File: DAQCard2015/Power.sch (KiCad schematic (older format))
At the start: 22 parts, among them CON1 BARREL_JACK, SW1 DPDT, U20 LM1086_1V8, U21 LT1913, U25 LM1086_2V5

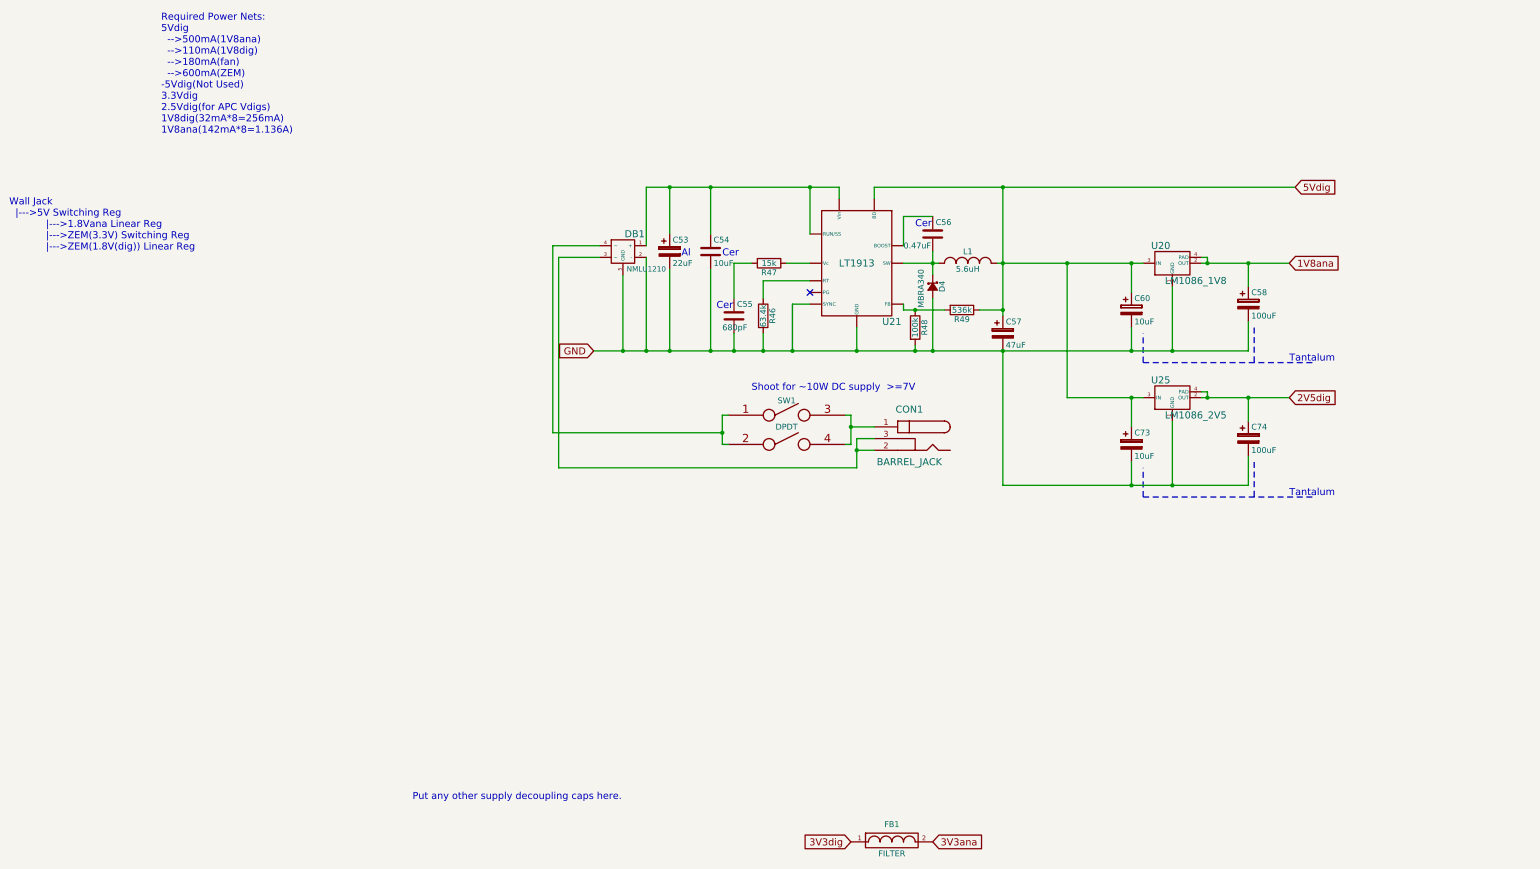
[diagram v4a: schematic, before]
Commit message: Adds digipart field to all parts that is now used in automatic generation of BOM(see DAQCard2015.html)
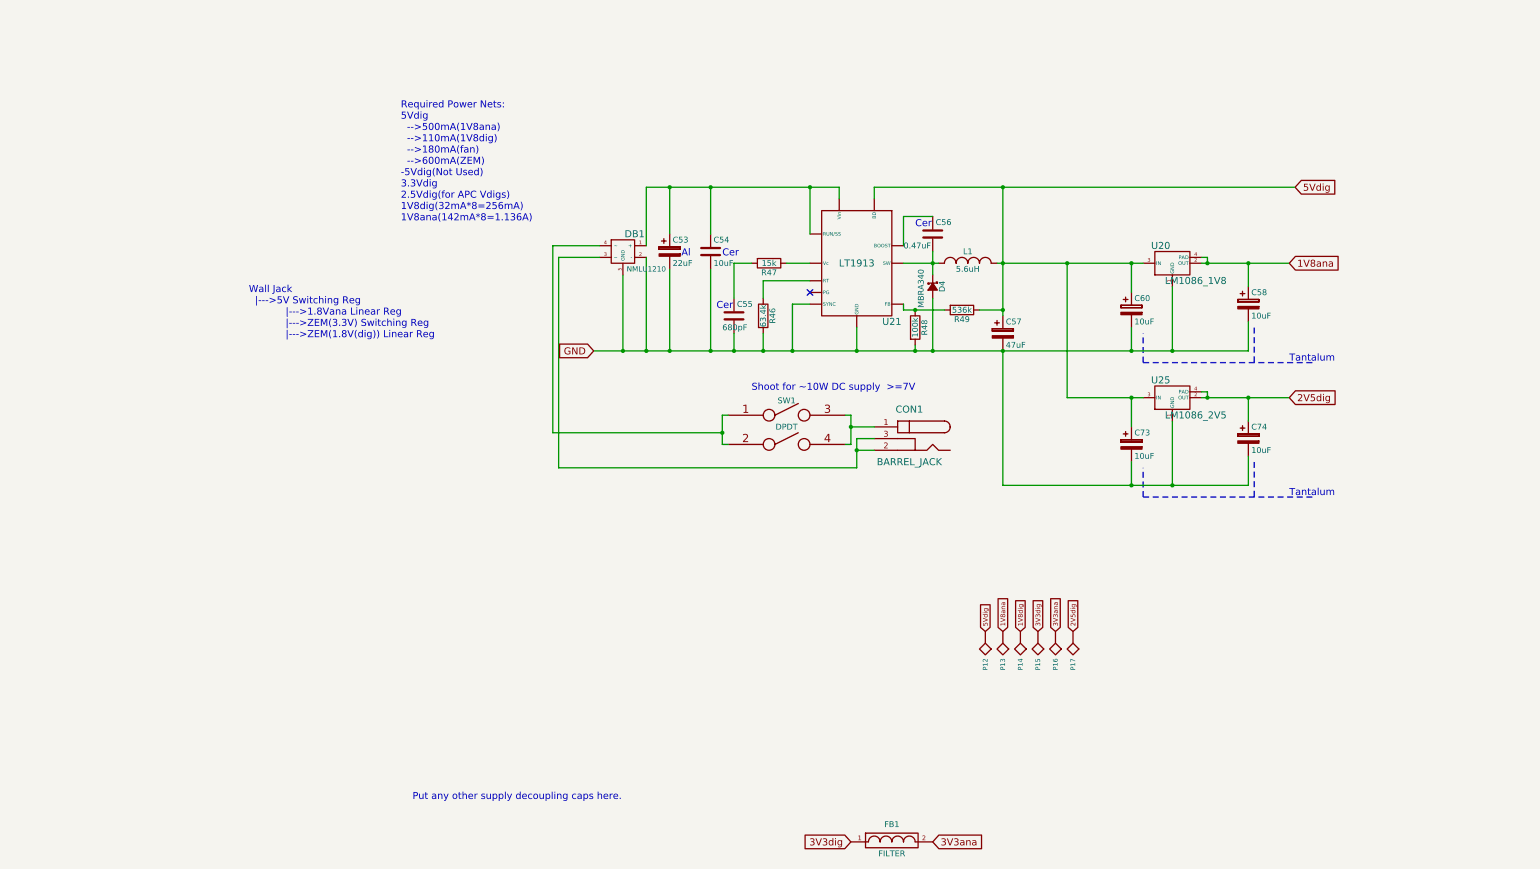
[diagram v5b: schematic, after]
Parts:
- added P12: 5Vdig, extras:testpad, symbol SPYPAD
- added P13: 1.8Vana, extras:testpad, symbol SPYPAD
- added P14: 1.8Vdig, extras:testpad, symbol SPYPAD
- added P15: 3.3Vdig, extras:testpad, symbol SPYPAD
- added P16: 3.3Vana, extras:testpad, symbol SPYPAD
- added P17: 2.5Vdig, extras:testpad, symbol SPYPAD
- C53: digipart (none) -> 493-9771-1-ND
- C54: digipart (none) -> 445-11464-1-ND
- C55: digipart (none) -> 445-1291-1-ND
- C56: digipart (none) -> 445-7464-1-ND
- C57: digipart (none) -> 478-9200-1-ND
- C58, C74: value 100uF -> 10uF; digipart (none) -> 478-3337-1-ND
- C60, C73: digipart (none) -> 478-3337-1-ND
- CON1: digipart (none) -> CP-002B-ND
- D4: digipart (none) -> MBRA340T3GOSCT-ND
- DB1: digipart (none) -> NMLU1210TWGOSCT-ND
- FB1: digipart (none) -> MH2029-070YCT-ND
- L1: digipart (none) -> 445-6477-1-ND
- R46: digipart (none) -> P63.4KHCT-ND
- R47: digipart (none) -> P15.0KHCT-ND
- R48: digipart (none) -> P100KHCT-ND
- R49: digipart (none) -> P536KHCT-ND
- SW1: digipart (none) -> CKN2062-ND
- U20: digipart (none) -> LM1086ISX-1.8/NOPBCT-ND
- U21: digipart (none) -> LT1913EDD#PBF-ND
- U25: digipart (none) -> LM1086CSX-2.5/NOPBCT-ND
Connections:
- net 1V8ana: now also P13.1
- net 2V5dig: now also P17.1
- net 3V3ana: now also P16.1
- net 3V3dig: now also P15.1
- net 5Vdig: now also P12.1
- new net 1V8dig: P14.1
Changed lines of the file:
@@
 Comment4 ""
 $EndDescr
-Text Notes -600 1050 0    60   ~ 0
+Text Notes 1450 1800 0    60   ~ 0
 Required Power Nets:\n5Vdig\n  -->500mA(1V8ana)\n  -->110mA(1V8dig)\n  -->180mA(fan)\n  -->600mA(ZEM)\n-5Vdig(Not Used)\n3.3Vdig\n2.5Vdig(for APC Vdigs)\n1V8dig(32mA*8=256mA)\n1V8ana(142mA*8=1.136A)
 Text GLabel 9050 2150 2    60   Input ~ 0
@@
 F 2 "Connect:BARREL_JACK" H 5800 3650 60  0001 C CNN
 F 3 "" H 5800 3650 60  0000 C CNN
+F 4 "CP-002B-ND" H 5800 3650 60  0001 C CNN "digipart"
 	1    5800 3650
 	-1   0    0    -1
@@
 F 2 "extras:SMD_Cap_8mmDia" H 3788 1900 30  0001 C CNN
 F 3 "" H 3750 2050 60  0000 C CNN
+F 4 "493-9771-1-ND" H 3750 2050 60  0001 C CNN "digipart"
 	1    3750 2050
 	1    0    0    -1
@@
 F 2 "Resistors_SMD:R_0805" H 5650 7100 60  0001 C CNN
 F 3 "" H 5650 7100 60  0000 C CNN
+F 4 "MH2029-070YCT-ND" H 5650 7100 60  0001 C CNN "digipart"
 	1    5650 7100
 	1    0    0    -1
@@
 F 2 "extras:TO-263-4" H 8050 2350 60  0001 C CNN
 F 3 "" H 8050 2350 60  0000 C CNN
+F 4 "LM1086ISX-1.8/NOPBCT-ND" H 8050 2350 60  0001 C CNN "digipart"
 	1    8050 2350
 	1    0    0    -1
@@
 F 2 "Capacitors_SMD:C_0805" H 4138 1900 30  0001 C CNN
 F 3 "" H 4100 2050 60  0000 C CNN
+F 4 "445-11464-1-ND" H 4100 2050 60  0001 C CNN "digipart"
 	1    4100 2050
 	1    0    0    -1
@@
 F 2 "extras:LT1913" H 3450 1700 60  0001 C CNN
 F 3 "" H 3450 1700 60  0000 C CNN
+F 4 "LT1913EDD#PBF-ND" H 5350 2150 60  0001 C CNN "digipart"
 	1    5350 2150
 	1    0    0    -1
@@
 F 2 "Capacitors_SMD:C_0603" H 4338 2450 30  0001 C CNN
 F 3 "" H 4300 2600 60  0000 C CNN
+F 4 "445-1291-1-ND" H 4300 2600 60  0001 C CNN "digipart"
 	1    4300 2600
 	1    0    0    -1
@@
 F 2 "Capacitors_SMD:C_0603" H 6038 1750 30  0001 C CNN
 F 3 "" H 6000 1900 60  0000 C CNN
+F 4 "445-7464-1-ND" H 6000 1900 60  0001 C CNN "digipart"
 	1    6000 1900
 	1    0    0    -1
@@
 F 2 "Resistors_SMD:R_0603" V 4530 2150 30  0001 C CNN
 F 3 "" H 4600 2150 30  0000 C CNN
+F 4 "P15.0KHCT-ND" V 4600 2150 60  0001 C CNN "digipart"
 	1    4600 2150
 	0    1    1    0
@@
 F 2 "Resistors_SMD:R_0603" V 4480 2600 30  0001 C CNN
 F 3 "" H 4550 2600 30  0000 C CNN
+F 4 "P63.4KHCT-ND" V 4550 2600 60  0001 C CNN "digipart"
 	1    4550 2600
 	1    0    0    -1
@@
 F 2 "Diodes_SMD:SMA_Standard" V 6000 2350 60  0001 C CNN
 F 3 "" V 6000 2350 60  0000 C CNN
+F 4 "MBRA340T3GOSCT-ND" H 6000 2350 60  0001 C CNN "digipart"
 	1    6000 2350
 	0    1    1    0
@@
 F 2 "Resistors_SMD:R_0603" V 5780 2700 30  0001 C CNN
 F 3 "" H 5850 2700 30  0000 C CNN
+F 4 "P100KHCT-ND" V 5850 2700 60  0001 C CNN "digipart"
 	1    5850 2700
 	1    0    0    -1
@@
 F 2 "Resistors_SMD:R_0603" V 6180 2550 30  0001 C CNN
 F 3 "" H 6250 2550 30  0000 C CNN
+F 4 "P536KHCT-ND" V 6250 2550 60  0001 C CNN "digipart"
 	1    6250 2550
 	0    1    1    0
@@
 F 2 "extras:SLF101" H 6300 2150 60  0001 C CNN
 F 3 "" H 6300 2150 60  0000 C CNN
+F 4 "445-6477-1-ND" H 6300 2150 60  0001 C CNN "digipart"
 	1    6300 2150
 	1    0    0    -1
 $EndComp
-Text Notes -1900 2050 0    60   ~ 0
+Text Notes 150  2800 0    60   ~ 0
 Wall Jack\n  |--->5V Switching Reg\n            |--->1.8Vana Linear Reg\n            |--->ZEM(3.3V) Switching Reg\n            |--->ZEM(1.8V(dig)) Linear Reg\n
 $Comp
@@
 F 2 "extras:NMLU1210" H 3250 1975 60  0001 C CNN
 F 3 "" H 3250 1975 60  0000 C CNN
+F 4 "NMLU1210TWGOSCT-ND" H 3350 2050 60  0001 C CNN "digipart"
 	1    3350 2050
 	-1   0    0    -1
@@
 P 8700 2500
 F 0 "C58" H 8725 2600 50  0000 L CNN
-F 1 "100uF" H 8725 2400 50  0000 L CNN
+F 1 "10uF" H 8725 2400 50  0000 L CNN
 F 2 "Capacitors_Tantalum_SMD:TantalC_SizeD_EIA-7343_Reflow" H 8738 2350 30  0001 C CNN
 F 3 "" H 8700 2500 60  0000 C CNN
+F 4 "478-3337-1-ND" H 8700 2500 60  0001 C CNN "digipart"
 	1    8700 2500
 	1    0    0    -1
@@
 F 2 "Capacitors_Tantalum_SMD:TantalC_SizeD_EIA-7343_Reflow" H 7738 2400 30  0001 C CNN
 F 3 "" H 7700 2550 60  0000 C CNN
+F 4 "478-3337-1-ND" H 7700 2550 60  0001 C CNN "digipart"
 	1    7700 2550
 	1    0    0    -1
@@
 F 2 "Capacitors_Tantalum_SMD:TantalC_SizeD_EIA-7343_Reflow" H 6638 2600 30  0001 C CNN
 F 3 "" H 6600 2750 60  0000 C CNN
+F 4 "478-9200-1-ND" H 6600 2750 60  0001 C CNN "digipart"
 	1    6600 2750
 	1    0    0    -1
@@
 F 2 "extras:TO-263-4" H 8050 3500 60  0001 C CNN
 F 3 "" H 8050 3500 60  0000 C CNN
+F 4 "LM1086CSX-2.5/NOPBCT-ND" H 8050 3500 60  0001 C CNN "digipart"
 	1    8050 3500
 	1    0    0    -1
@@
 P 8700 3650
 F 0 "C74" H 8725 3750 50  0000 L CNN
-F 1 "100uF" H 8725 3550 50  0000 L CNN
+F 1 "10uF" H 8725 3550 50  0000 L CNN
 F 2 "Capacitors_Tantalum_SMD:TantalC_SizeD_EIA-7343_Reflow" H 8738 3500 30  0001 C CNN
 F 3 "" H 8700 3650 60  0000 C CNN
+F 4 "478-3337-1-ND" H 8700 3650 60  0001 C CNN "digipart"
 	1    8700 3650
 	1    0    0    -1
@@
 F 2 "Capacitors_Tantalum_SMD:TantalC_SizeD_EIA-7343_Reflow" H 7738 3550 30  0001 C CNN
 F 3 "" H 7700 3700 60  0000 C CNN
+F 4 "478-3337-1-ND" H 7700 3700 60  0001 C CNN "digipart"
 	1    7700 3700
 	1    0    0    -1
@@
 F 2 "extras:DFXX-XX-X-XX-A-X-XX" H 4750 3450 60  0001 C CNN
 F 3 "" H 4750 3450 60  0000 C CNN
+F 4 "CKN2062-ND" H 4750 3450 60  0001 C CNN "digipart"
 	1    4750 3450
 	1    0    0    -1
@@
 Wire Wire Line
 	2800 3900 2800 2100
+$Comp
+L SPYPAD P12
+U 1 1 560EDBF6
+P 6450 5450
+F 0 "P12" H 6530 5450 40  0000 L CNN
+F 1 "5Vdig" H 6450 5500 30  0001 C CNN
+F 2 "extras:testpad" H 6450 5450 60  0001 C CNN
+F 3 "" H 6450 5450 60  0000 C CNN
+	1    6450 5450
+	0    1    1    0
+$EndComp
+$Comp
+L SPYPAD P13
+U 1 1 560EDD25
+P 6600 5450
+F 0 "P13" H 6680 5450 40  0000 L CNN
+F 1 "1.8Vana" H 6600 5500 30  0001 C CNN
+F 2 "extras:testpad" H 6600 5450 60  0001 C CNN
+F 3 "" H 6600 5450 60  0000 C CNN
+	1    6600 5450
+	0    1    1    0
+$EndComp
+$Comp
+L SPYPAD P14
+U 1 1 560EDD7F
+P 6750 5450
+F 0 "P14" H 6830 5450 40  0000 L CNN
+F 1 "1.8Vdig" H 6750 5500 30  0001 C CNN
+F 2 "extras:testpad" H 6750 5450 60  0001 C CNN
+F 3 "" H 6750 5450 60  0000 C CNN
+	1    6750 5450
+	0    1    1    0
+$EndComp
+$Comp
+L SPYPAD P15
+U 1 1 560EDDDC
+P 6900 5450
+F 0 "P15" H 6980 5450 40  0000 L CNN
+F 1 "3.3Vdig" H 6900 5500 30  0001 C CNN
+F 2 "extras:testpad" H 6900 5450 60  0001 C CNN
+F 3 "" H 6900 5450 60  0000 C CNN
+	1    6900 5450
+	0    1    1    0
+$EndComp
+$Comp
+L SPYPAD P16
+U 1 1 560EDE3C
+P 7050 5450
+F 0 "P16" H 7130 5450 40  0000 L CNN
+F 1 "3.3Vana" H 7050 5500 30  0001 C CNN
+F 2 "extras:testpad" H 7050 5450 60  0001 C CNN
+F 3 "" H 7050 5450 60  0000 C CNN
+	1    7050 5450
+	0    1    1    0
+$EndComp
+Text GLabel 6450 5300 1    40   Input ~ 0
+5Vdig
+Text GLabel 6600 5300 1    40   Input ~ 0
+1V8ana
+Text GLabel 6750 5300 1    40   Input ~ 0
+1V8dig
+Text GLabel 6900 5300 1    40   Input ~ 0
+3V3dig
+Text GLabel 7050 5300 1    40   Input ~ 0
+3V3ana
+$Comp
+L SPYPAD P17
+U 1 1 560EE37C
+P 7200 5450
+F 0 "P17" H 7280 5450 40  0000 L CNN
+F 1 "2.5Vdig" H 7200 5500 30  0001 C CNN
+F 2 "extras:testpad" H 7200 5450 60  0001 C CNN
+F 3 "" H 7200 5450 60  0000 C CNN
+	1    7200 5450
+	0    1    1    0
+$EndComp
+Text GLabel 7200 5300 1    40   Input ~ 0
+2V5dig
 $EndSCHEMATC

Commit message: bunch of updates
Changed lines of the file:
@@
 	8300 2100 8350 2100
-Wire Wire Line
-	6550 2150 7800 2150
 Wire Wire Line
 	2800 2100 3150 2100
@@
 Wire Notes Line
 	7800 3000 7800 2750
-Wire Wire Line
-	3100 2900 8700 2900
 $Comp
 L CP C57
@@
 	6600 4050 8700 4050
 Wire Wire Line
-	7150 3300 7150 2150
+	7150 1500 7150 3300
 Connection ~ 7150 2150
 Wire Wire Line
@@
 Text GLabel 7200 5300 1    40   Input ~ 0
 2V5dig
+Wire Wire Line
+	6550 2150 6600 2150
+Connection ~ 7150 1500
+Wire Wire Line
+	7150 2150 7800 2150
+Wire Wire Line
+	3100 2900 8700 2900
 $EndSCHEMATC

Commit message: annotates parts for new build-management tool
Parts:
- C53: Digikey (none) -> 493-9771-1-ND; digipart 493-9771-1-ND -> (none)
- C54: Digikey (none) -> 445-11464-1-ND; digipart 445-11464-1-ND -> (none)
- C55: Digikey (none) -> 445-1291-1-ND; digipart 445-1291-1-ND -> (none)
- C56: Digikey (none) -> 445-7464-1-ND; digipart 445-7464-1-ND -> (none)
- C57: Digikey (none) -> 478-9200-1-ND; digipart 478-9200-1-ND -> (none)
- C58, C60, C73, C74: Digikey (none) -> 478-3337-1-ND; digipart 478-3337-1-ND -> (none)
- CON1: Digikey (none) -> CP-002B-ND; digipart CP-002B-ND -> (none)
- D4: Digikey (none) -> MBRA340T3GOSCT-ND; digipart MBRA340T3GOSCT-ND -> (none)
- DB1: Digikey (none) -> NMLU1210TWGOSCT-ND; digipart NMLU1210TWGOSCT-ND -> (none)
- FB1: Digikey (none) -> MH2029-070YCT-ND; digipart MH2029-070YCT-ND -> (none)
- L1: Digikey (none) -> 445-6477-1-ND; digipart 445-6477-1-ND -> (none)
- R46: Digikey (none) -> P63.4KHCT-ND; digipart P63.4KHCT-ND -> (none)
- R47: Digikey (none) -> P15.0KHCT-ND; digipart P15.0KHCT-ND -> (none)
- R48: Digikey (none) -> P100KHCT-ND; digipart P100KHCT-ND -> (none)
- R49: Digikey (none) -> P536KHCT-ND; digipart P536KHCT-ND -> (none)
- SW1: Digikey (none) -> CKN2062-ND; digipart CKN2062-ND -> (none)
- U20: Digikey (none) -> LM1086ISX-1.8/NOPBCT-ND; digipart LM1086ISX-1.8/NOPBCT-ND -> (none)
- U21: Digikey (none) -> LT1913EDD#PBF-ND; digipart LT1913EDD#PBF-ND -> (none)
- U25: Digikey (none) -> LM1086CSX-2.5/NOPBCT-ND; digipart LM1086CSX-2.5/NOPBCT-ND -> (none)
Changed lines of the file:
@@
 EESchema Schematic File Version 2
+LIBS:DAQCard2015-rescue
 LIBS:power
 LIBS:device
@@
 F 2 "Connect:BARREL_JACK" H 5800 3650 60  0001 C CNN
 F 3 "" H 5800 3650 60  0000 C CNN
-F 4 "CP-002B-ND" H 5800 3650 60  0001 C CNN "digipart"
+F 4 "CP-002B-ND" H 5800 3650 60  0001 C CNN "Digikey"
 	1    5800 3650
 	-1   0    0    -1
@@
 F 2 "extras:SMD_Cap_8mmDia" H 3788 1900 30  0001 C CNN
 F 3 "" H 3750 2050 60  0000 C CNN
-F 4 "493-9771-1-ND" H 3750 2050 60  0001 C CNN "digipart"
+F 4 "493-9771-1-ND" H 3750 2050 60  0001 C CNN "Digikey"
 	1    3750 2050
 	1    0    0    -1
@@
 F 2 "Resistors_SMD:R_0805" H 5650 7100 60  0001 C CNN
 F 3 "" H 5650 7100 60  0000 C CNN
-F 4 "MH2029-070YCT-ND" H 5650 7100 60  0001 C CNN "digipart"
+F 4 "MH2029-070YCT-ND" H 5650 7100 60  0001 C CNN "Digikey"
 	1    5650 7100
 	1    0    0    -1
@@
 F 2 "extras:TO-263-4" H 8050 2350 60  0001 C CNN
 F 3 "" H 8050 2350 60  0000 C CNN
-F 4 "LM1086ISX-1.8/NOPBCT-ND" H 8050 2350 60  0001 C CNN "digipart"
+F 4 "LM1086ISX-1.8/NOPBCT-ND" H 8050 2350 60  0001 C CNN "Digikey"
 	1    8050 2350
 	1    0    0    -1
@@
 F 2 "Capacitors_SMD:C_0805" H 4138 1900 30  0001 C CNN
 F 3 "" H 4100 2050 60  0000 C CNN
-F 4 "445-11464-1-ND" H 4100 2050 60  0001 C CNN "digipart"
+F 4 "445-11464-1-ND" H 4100 2050 60  0001 C CNN "Digikey"
 	1    4100 2050
 	1    0    0    -1
@@
 F 2 "extras:LT1913" H 3450 1700 60  0001 C CNN
 F 3 "" H 3450 1700 60  0000 C CNN
-F 4 "LT1913EDD#PBF-ND" H 5350 2150 60  0001 C CNN "digipart"
+F 4 "LT1913EDD#PBF-ND" H 5350 2150 60  0001 C CNN "Digikey"
 	1    5350 2150
 	1    0    0    -1
@@
 F 2 "Capacitors_SMD:C_0603" H 4338 2450 30  0001 C CNN
 F 3 "" H 4300 2600 60  0000 C CNN
-F 4 "445-1291-1-ND" H 4300 2600 60  0001 C CNN "digipart"
+F 4 "445-1291-1-ND" H 4300 2600 60  0001 C CNN "Digikey"
 	1    4300 2600
 	1    0    0    -1
@@
 F 2 "Capacitors_SMD:C_0603" H 6038 1750 30  0001 C CNN
 F 3 "" H 6000 1900 60  0000 C CNN
-F 4 "445-7464-1-ND" H 6000 1900 60  0001 C CNN "digipart"
+F 4 "445-7464-1-ND" H 6000 1900 60  0001 C CNN "Digikey"
 	1    6000 1900
 	1    0    0    -1
@@
 F 2 "Resistors_SMD:R_0603" V 4530 2150 30  0001 C CNN
 F 3 "" H 4600 2150 30  0000 C CNN
-F 4 "P15.0KHCT-ND" V 4600 2150 60  0001 C CNN "digipart"
+F 4 "P15.0KHCT-ND" V 4600 2150 60  0001 C CNN "Digikey"
 	1    4600 2150
 	0    1    1    0
@@
 F 2 "Resistors_SMD:R_0603" V 4480 2600 30  0001 C CNN
 F 3 "" H 4550 2600 30  0000 C CNN
-F 4 "P63.4KHCT-ND" V 4550 2600 60  0001 C CNN "digipart"
+F 4 "P63.4KHCT-ND" V 4550 2600 60  0001 C CNN "Digikey"
 	1    4550 2600
 	1    0    0    -1
@@
 F 2 "Diodes_SMD:SMA_Standard" V 6000 2350 60  0001 C CNN
 F 3 "" V 6000 2350 60  0000 C CNN
-F 4 "MBRA340T3GOSCT-ND" H 6000 2350 60  0001 C CNN "digipart"
+F 4 "MBRA340T3GOSCT-ND" H 6000 2350 60  0001 C CNN "Digikey"
 	1    6000 2350
 	0    1    1    0
@@
 F 2 "Resistors_SMD:R_0603" V 5780 2700 30  0001 C CNN
 F 3 "" H 5850 2700 30  0000 C CNN
-F 4 "P100KHCT-ND" V 5850 2700 60  0001 C CNN "digipart"
+F 4 "P100KHCT-ND" V 5850 2700 60  0001 C CNN "Digikey"
 	1    5850 2700
 	1    0    0    -1
@@
 F 2 "Resistors_SMD:R_0603" V 6180 2550 30  0001 C CNN
 F 3 "" H 6250 2550 30  0000 C CNN
-F 4 "P536KHCT-ND" V 6250 2550 60  0001 C CNN "digipart"
+F 4 "P536KHCT-ND" V 6250 2550 60  0001 C CNN "Digikey"
 	1    6250 2550
 	0    1    1    0
@@
 F 2 "extras:SLF101" H 6300 2150 60  0001 C CNN
 F 3 "" H 6300 2150 60  0000 C CNN
-F 4 "445-6477-1-ND" H 6300 2150 60  0001 C CNN "digipart"
+F 4 "445-6477-1-ND" H 6300 2150 60  0001 C CNN "Digikey"
 	1    6300 2150
 	1    0    0    -1
@@
 F 2 "extras:NMLU1210" H 3250 1975 60  0001 C CNN
 F 3 "" H 3250 1975 60  0000 C CNN
-F 4 "NMLU1210TWGOSCT-ND" H 3350 2050 60  0001 C CNN "digipart"
+F 4 "NMLU1210TWGOSCT-ND" H 3350 2050 60  0001 C CNN "Digikey"
 	1    3350 2050
 	-1   0    0    -1
@@
 F 2 "Capacitors_Tantalum_SMD:TantalC_SizeD_EIA-7343_Reflow" H 8738 2350 30  0001 C CNN
 F 3 "" H 8700 2500 60  0000 C CNN
-F 4 "478-3337-1-ND" H 8700 2500 60  0001 C CNN "digipart"
+F 4 "478-3337-1-ND" H 8700 2500 60  0001 C CNN "Digikey"
 	1    8700 2500
 	1    0    0    -1
@@
 F 2 "Capacitors_Tantalum_SMD:TantalC_SizeD_EIA-7343_Reflow" H 7738 2400 30  0001 C CNN
 F 3 "" H 7700 2550 60  0000 C CNN
-F 4 "478-3337-1-ND" H 7700 2550 60  0001 C CNN "digipart"
+F 4 "478-3337-1-ND" H 7700 2550 60  0001 C CNN "Digikey"
 	1    7700 2550
 	1    0    0    -1
@@
 F 2 "Capacitors_Tantalum_SMD:TantalC_SizeD_EIA-7343_Reflow" H 6638 2600 30  0001 C CNN
 F 3 "" H 6600 2750 60  0000 C CNN
-F 4 "478-9200-1-ND" H 6600 2750 60  0001 C CNN "digipart"
+F 4 "478-9200-1-ND" H 6600 2750 60  0001 C CNN "Digikey"
 	1    6600 2750
 	1    0    0    -1
@@
 F 2 "extras:TO-263-4" H 8050 3500 60  0001 C CNN
 F 3 "" H 8050 3500 60  0000 C CNN
-F 4 "LM1086CSX-2.5/NOPBCT-ND" H 8050 3500 60  0001 C CNN "digipart"
+F 4 "LM1086CSX-2.5/NOPBCT-ND" H 8050 3500 60  0001 C CNN "Digikey"
 	1    8050 3500
 	1    0    0    -1
@@
 F 2 "Capacitors_Tantalum_SMD:TantalC_SizeD_EIA-7343_Reflow" H 8738 3500 30  0001 C CNN
 F 3 "" H 8700 3650 60  0000 C CNN
-F 4 "478-3337-1-ND" H 8700 3650 60  0001 C CNN "digipart"
+F 4 "478-3337-1-ND" H 8700 3650 60  0001 C CNN "Digikey"
 	1    8700 3650
 	1    0    0    -1
@@
 F 2 "Capacitors_Tantalum_SMD:TantalC_SizeD_EIA-7343_Reflow" H 7738 3550 30  0001 C CNN
 F 3 "" H 7700 3700 60  0000 C CNN
-F 4 "478-3337-1-ND" H 7700 3700 60  0001 C CNN "digipart"
+F 4 "478-3337-1-ND" H 7700 3700 60  0001 C CNN "Digikey"
 	1    7700 3700
 	1    0    0    -1
@@
 F 2 "extras:DFXX-XX-X-XX-A-X-XX" H 4750 3450 60  0001 C CNN
 F 3 "" H 4750 3450 60  0000 C CNN
-F 4 "CKN2062-ND" H 4750 3450 60  0001 C CNN "digipart"
+F 4 "CKN2062-ND" H 4750 3450 60  0001 C CNN "Digikey"
 	1    4750 3450
 	1    0    0    -1
